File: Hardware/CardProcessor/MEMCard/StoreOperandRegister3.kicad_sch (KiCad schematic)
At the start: 3 parts, among them U15 74ABT16245

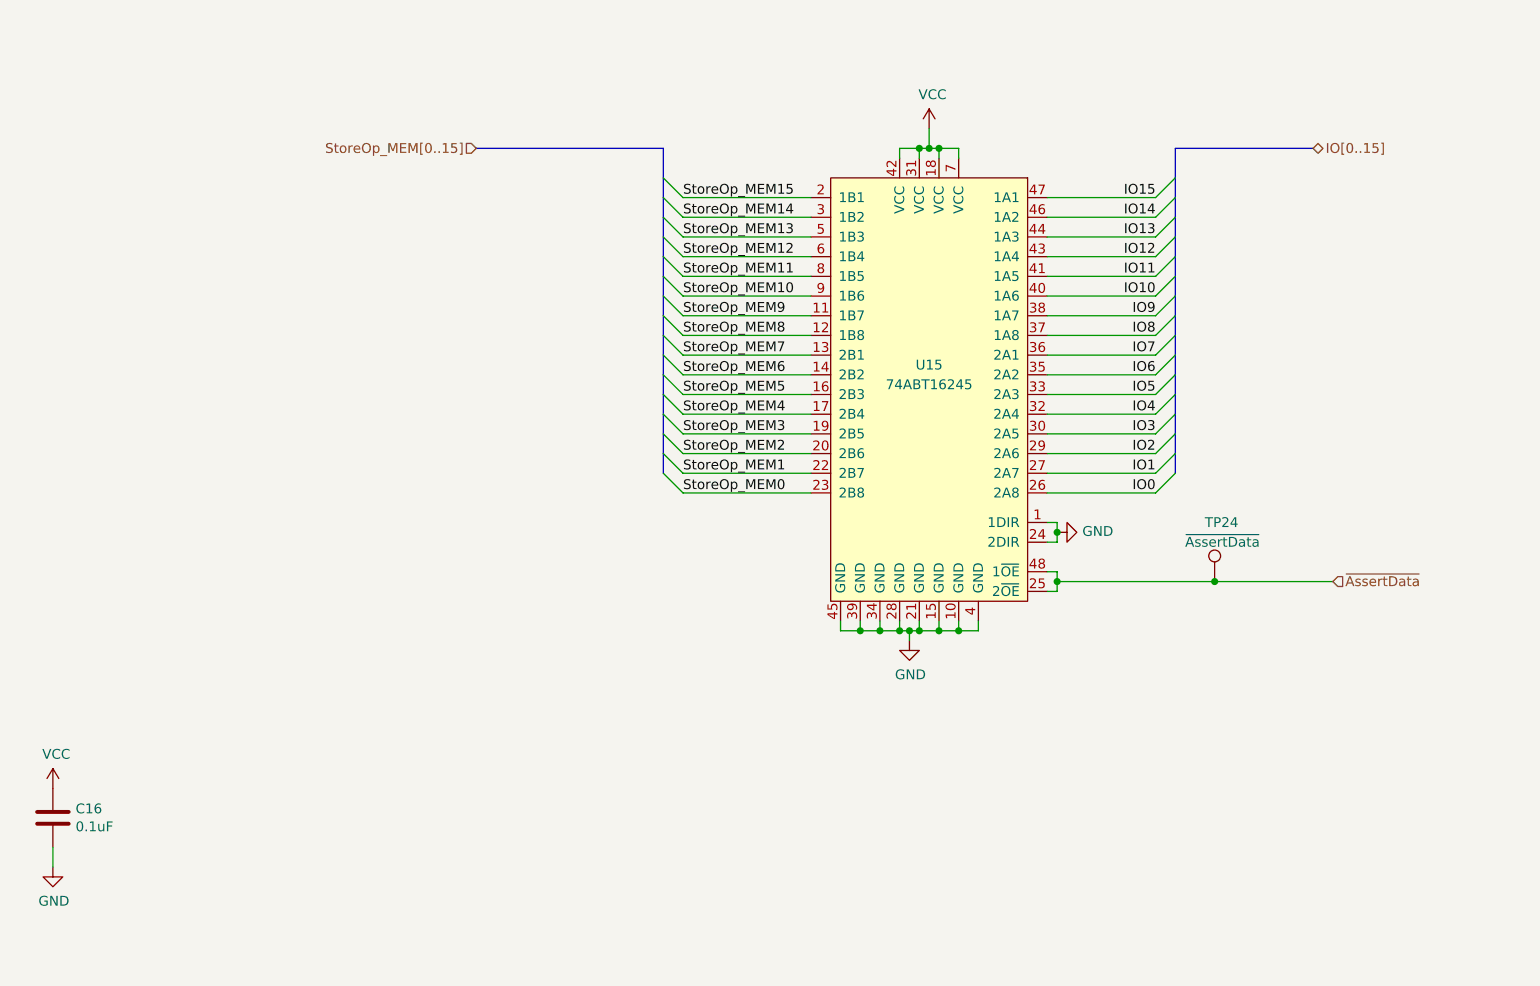
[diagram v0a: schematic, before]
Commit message: Rename MEMModule to MEMCard
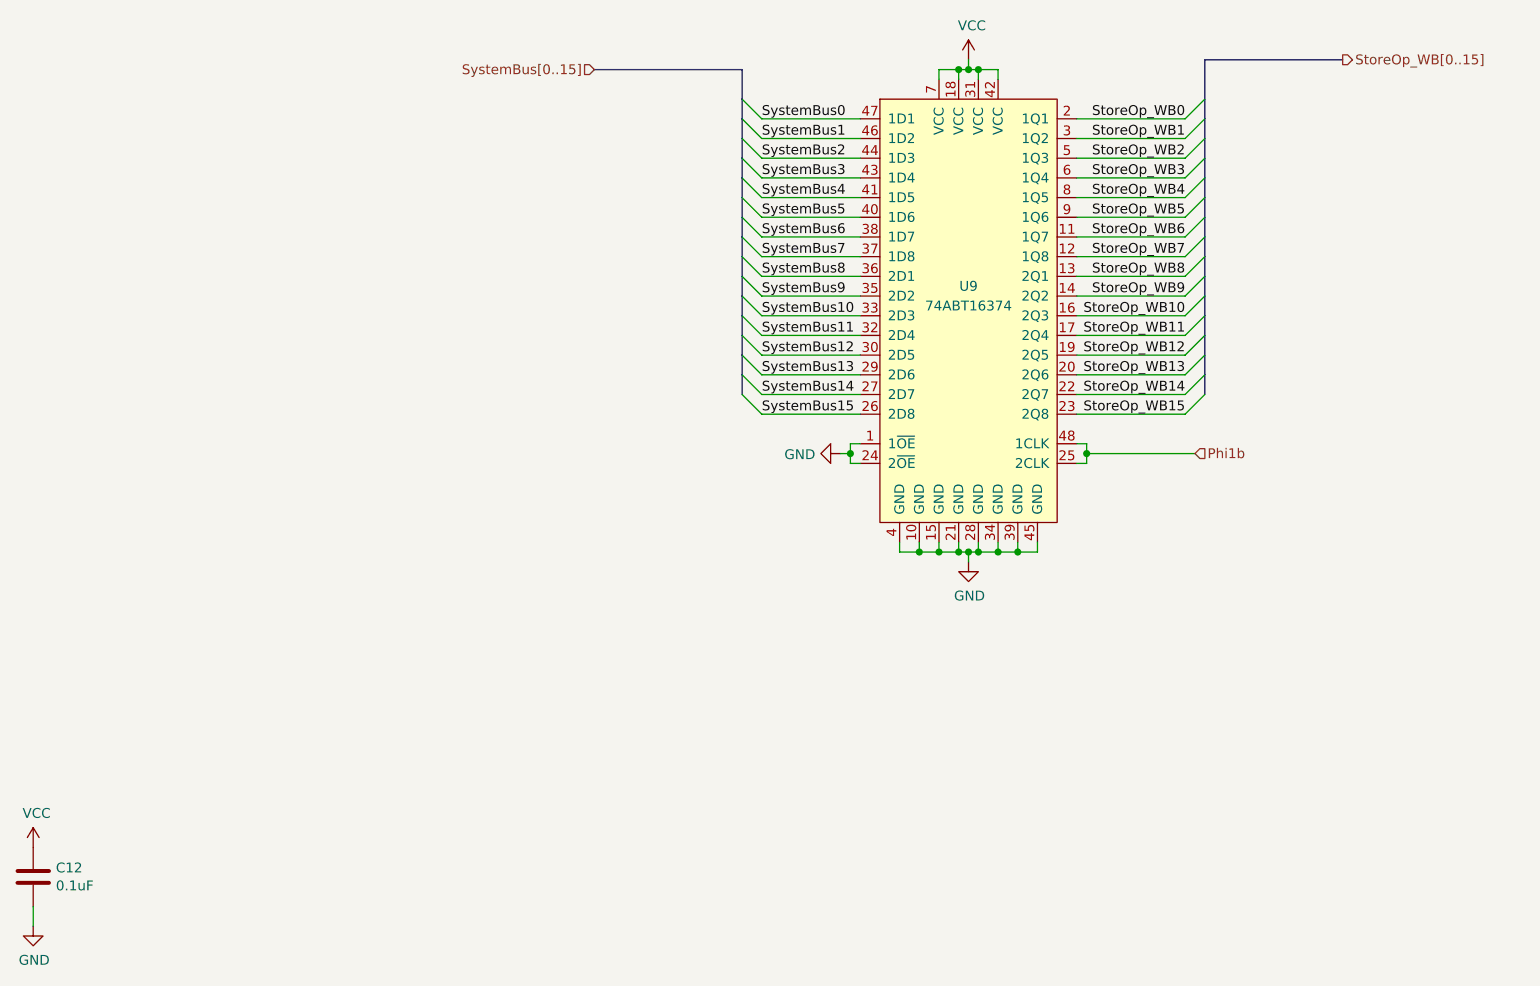
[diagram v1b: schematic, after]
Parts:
- removed C16: 0.1uF, Capacitor_SMD:C_0603_1608Metric, symbol Device:C
- removed TP24: ~{AssertData}, TestPoint:TestPoint_Pad_D1.0mm, symbol Connector:TestPoint
- removed U15: 74ABT16245, Package_SO:TSSOP-48_6.1x12.5mm_P0.5mm, symbol Turtle16:74ABT16245
- added C12: 0.1uF, Capacitor_SMD:C_0603_1608Metric, symbol Device:C
- added U9: 74ABT16374, Package_SO:TSSOP-48_6.1x12.5mm_P0.5mm, symbol Turtle16:74ABT16374
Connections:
- net GND: now also C12.2, U9.1 (1~{OE}), U9.10 (GND), U9.15 (GND), U9.21 (GND), U9.24 (2~{OE}), U9.28 (GND), U9.34 (GND), U9.39 (GND), U9.4 (GND), U9.45 (GND)
- net VCC: now also C12.1, U9.18 (VCC), U9.31 (VCC), U9.42 (VCC), U9.7 (VCC)
- new net Phi1b: U9.25 (2CLK), U9.48 (1CLK)
- new net StoreOp_WB0: U9.2 (1Q1)
- new net StoreOp_WB1: U9.3 (1Q2)
- new net StoreOp_WB10: U9.16 (2Q3)
- new net StoreOp_WB11: U9.17 (2Q4)
- new net StoreOp_WB12: U9.19 (2Q5)
- new net StoreOp_WB13: U9.20 (2Q6)
- new net StoreOp_WB14: U9.22 (2Q7)
- new net StoreOp_WB15: U9.23 (2Q8)
- new net StoreOp_WB2: U9.5 (1Q3)
- new net StoreOp_WB3: U9.6 (1Q4)
- new net StoreOp_WB4: U9.8 (1Q5)
- new net StoreOp_WB5: U9.9 (1Q6)
- new net StoreOp_WB6: U9.11 (1Q7)
- new net StoreOp_WB7: U9.12 (1Q8)
- new net StoreOp_WB8: U9.13 (2Q1)
- new net StoreOp_WB9: U9.14 (2Q2)
- new net SystemBus0: U9.47 (1D1)
- new net SystemBus1: U9.46 (1D2)
- new net SystemBus10: U9.33 (2D3)
- new net SystemBus11: U9.32 (2D4)
- new net SystemBus12: U9.30 (2D5)
- new net SystemBus13: U9.29 (2D6)
- new net SystemBus14: U9.27 (2D7)
- new net SystemBus15: U9.26 (2D8)
- new net SystemBus2: U9.44 (1D3)
- new net SystemBus3: U9.43 (1D4)
- new net SystemBus4: U9.41 (1D5)
- new net SystemBus5: U9.40 (1D6)
- new net SystemBus6: U9.38 (1D7)
- new net SystemBus7: U9.37 (1D8)
- new net SystemBus8: U9.36 (2D1)
- new net SystemBus9: U9.35 (2D2)
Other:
- title: MEM: Buffer StoreOp -> MEM/WB: Store Operand Register

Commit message: Add Turtle16Computer, a KiCad project which has schematics for the computer as a whole
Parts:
- renumbered C12 to C9
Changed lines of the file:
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@@
 		(on_board yes)
 		(dnp no)
-		(property "Reference" "C12"
+		(property "Reference" "C?"
 			(at 24.511 180.4416 0)
 			(effects
@@
 		)
 		(instances
-			(project "MEMModule"
-				(path "/0734fc7f-a6cc-4e6e-9f39-47607536bc96/f77653f6-20ed-4160-b6ab-9e3d62667a68/00000000-0000-0000-0000-00005fd56bfa"
-					(reference "C12")
-					(unit 1)
-				)
-			)
-			(project "MainBoard"
-				(path "/83c5181e-f5ee-453c-ae5c-d7256ba8837d/278b84b0-d28f-4248-8f63-f89f14b1dc97/f77653f6-20ed-4160-b6ab-9e3d62667a68/00000000-0000-0000-0000-00005fd56bfa"
+			(project "MEMCard"
+				(path "/0734fc7f-a6cc-4e6e-9f39-47607536bc96/15226c01-8e12-4b81-9562-5f5a5e30fa57/689a64e6-039c-45af-97e3-58741a934fce/00000000-0000-0000-0000-00005fd56bfa"
+					(reference "C9")
+					(unit 1)
+				)
+			)
+			(project "MEMCard"
+				(path "/83c5181e-f5ee-453c-ae5c-d7256ba8837d/278b84b0-d28f-4248-8f63-f89f14b1dc97/689a64e6-039c-45af-97e3-58741a934fce/00000000-0000-0000-0000-00005fd56bfa"
 					(reference "C?")
 					(unit 1)
@@
 		(on_board yes)
 		(dnp no)
-		(property "Reference" "#PWR075"
+		(property "Reference" "#PWR?"
 			(at 21.59 181.61 0)
 			(effects
@@
 		)
 		(instances
-			(project "MEMModule"
-				(path "/0734fc7f-a6cc-4e6e-9f39-47607536bc96/f77653f6-20ed-4160-b6ab-9e3d62667a68/00000000-0000-0000-0000-00005fd56bfa"
-					(reference "#PWR075")
-					(unit 1)
-				)
-			)
-			(project "MainBoard"
-				(path "/83c5181e-f5ee-453c-ae5c-d7256ba8837d/278b84b0-d28f-4248-8f63-f89f14b1dc97/f77653f6-20ed-4160-b6ab-9e3d62667a68/00000000-0000-0000-0000-00005fd56bfa"
+			(project "MEMCard"
+				(path "/0734fc7f-a6cc-4e6e-9f39-47607536bc96/15226c01-8e12-4b81-9562-5f5a5e30fa57/689a64e6-039c-45af-97e3-58741a934fce/00000000-0000-0000-0000-00005fd56bfa"
+					(reference "#PWR046")
+					(unit 1)
+				)
+			)
+			(project "MEMCard"
+				(path "/83c5181e-f5ee-453c-ae5c-d7256ba8837d/278b84b0-d28f-4248-8f63-f89f14b1dc97/689a64e6-039c-45af-97e3-58741a934fce/00000000-0000-0000-0000-00005fd56bfa"
 					(reference "#PWR?")
 					(unit 1)
@@
 		(on_board yes)
 		(dnp no)
-		(property "Reference" "#PWR076"
+		(property "Reference" "#PWR?"
 			(at 21.59 194.31 0)
 			(effects
@@
 		)
 		(instances
-			(project "MEMModule"
-				(path "/0734fc7f-a6cc-4e6e-9f39-47607536bc96/f77653f6-20ed-4160-b6ab-9e3d62667a68/00000000-0000-0000-0000-00005fd56bfa"
-					(reference "#PWR076")
-					(unit 1)
-				)
-			)
-			(project "MainBoard"
-				(path "/83c5181e-f5ee-453c-ae5c-d7256ba8837d/278b84b0-d28f-4248-8f63-f89f14b1dc97/f77653f6-20ed-4160-b6ab-9e3d62667a68/00000000-0000-0000-0000-00005fd56bfa"
+			(project "MEMCard"
+				(path "/0734fc7f-a6cc-4e6e-9f39-47607536bc96/15226c01-8e12-4b81-9562-5f5a5e30fa57/689a64e6-039c-45af-97e3-58741a934fce/00000000-0000-0000-0000-00005fd56bfa"
+					(reference "#PWR047")
+					(unit 1)
+				)
+			)
+			(project "MEMCard"
+				(path "/83c5181e-f5ee-453c-ae5c-d7256ba8837d/278b84b0-d28f-4248-8f63-f89f14b1dc97/689a64e6-039c-45af-97e3-58741a934fce/00000000-0000-0000-0000-00005fd56bfa"
 					(reference "#PWR?")
 					(unit 1)
@@
 		(on_board yes)
 		(dnp no)
-		(property "Reference" "#PWR077"
+		(property "Reference" "#PWR?"
 			(at 119.38 127 0)
 			(effects
@@
 		)
 		(instances
-			(project "MEMModule"
-				(path "/0734fc7f-a6cc-4e6e-9f39-47607536bc96/f77653f6-20ed-4160-b6ab-9e3d62667a68/00000000-0000-0000-0000-00005fd56bfa"
-					(reference "#PWR077")
-					(unit 1)
-				)
-			)
-			(project "MainBoard"
-				(path "/83c5181e-f5ee-453c-ae5c-d7256ba8837d/278b84b0-d28f-4248-8f63-f89f14b1dc97/f77653f6-20ed-4160-b6ab-9e3d62667a68/00000000-0000-0000-0000-00005fd56bfa"
+			(project "MEMCard"
+				(path "/0734fc7f-a6cc-4e6e-9f39-47607536bc96/15226c01-8e12-4b81-9562-5f5a5e30fa57/689a64e6-039c-45af-97e3-58741a934fce/00000000-0000-0000-0000-00005fd56bfa"
+					(reference "#PWR048")
+					(unit 1)
+				)
+			)
+			(project "MEMCard"
+				(path "/83c5181e-f5ee-453c-ae5c-d7256ba8837d/278b84b0-d28f-4248-8f63-f89f14b1dc97/689a64e6-039c-45af-97e3-58741a934fce/00000000-0000-0000-0000-00005fd56bfa"
 					(reference "#PWR?")
 					(unit 1)
@@
 		(on_board yes)
 		(dnp no)
-		(property "Reference" "#PWR078"
+		(property "Reference" "#PWR?"
 			(at 142.24 80.01 0)
 			(effects
@@
 		)
 		(instances
-			(project "MEMModule"
-				(path "/0734fc7f-a6cc-4e6e-9f39-47607536bc96/f77653f6-20ed-4160-b6ab-9e3d62667a68/00000000-0000-0000-0000-00005fd56bfa"
-					(reference "#PWR078")
-					(unit 1)
-				)
-			)
-			(project "MainBoard"
-				(path "/83c5181e-f5ee-453c-ae5c-d7256ba8837d/278b84b0-d28f-4248-8f63-f89f14b1dc97/f77653f6-20ed-4160-b6ab-9e3d62667a68/00000000-0000-0000-0000-00005fd56bfa"
+			(project "MEMCard"
+				(path "/0734fc7f-a6cc-4e6e-9f39-47607536bc96/15226c01-8e12-4b81-9562-5f5a5e30fa57/689a64e6-039c-45af-97e3-58741a934fce/00000000-0000-0000-0000-00005fd56bfa"
+					(reference "#PWR049")
+					(unit 1)
+				)
+			)
+			(project "MEMCard"
+				(path "/83c5181e-f5ee-453c-ae5c-d7256ba8837d/278b84b0-d28f-4248-8f63-f89f14b1dc97/689a64e6-039c-45af-97e3-58741a934fce/00000000-0000-0000-0000-00005fd56bfa"
 					(reference "#PWR?")
 					(unit 1)
@@
 		(on_board yes)
 		(dnp no)
-		(property "Reference" "#PWR079"
+		(property "Reference" "#PWR?"
 			(at 142.24 147.32 0)
 			(effects
@@
 		)
 		(instances
-			(project "MEMModule"
-				(path "/0734fc7f-a6cc-4e6e-9f39-47607536bc96/f77653f6-20ed-4160-b6ab-9e3d62667a68/00000000-0000-0000-0000-00005fd56bfa"
-					(reference "#PWR079")
-					(unit 1)
-				)
-			)
-			(project "MainBoard"
-				(path "/83c5181e-f5ee-453c-ae5c-d7256ba8837d/278b84b0-d28f-4248-8f63-f89f14b1dc97/f77653f6-20ed-4160-b6ab-9e3d62667a68/00000000-0000-0000-0000-00005fd56bfa"
+			(project "MEMCard"
+				(path "/0734fc7f-a6cc-4e6e-9f39-47607536bc96/15226c01-8e12-4b81-9562-5f5a5e30fa57/689a64e6-039c-45af-97e3-58741a934fce/00000000-0000-0000-0000-00005fd56bfa"
+					(reference "#PWR050")
+					(unit 1)
+				)
+			)
+			(project "MEMCard"
+				(path "/83c5181e-f5ee-453c-ae5c-d7256ba8837d/278b84b0-d28f-4248-8f63-f89f14b1dc97/689a64e6-039c-45af-97e3-58741a934fce/00000000-0000-0000-0000-00005fd56bfa"
 					(reference "#PWR?")
 					(unit 1)
@@
 		(on_board yes)
 		(dnp no)
-		(property "Reference" "U9"
+		(property "Reference" "U?"
 			(at 142.24 105.41 0)
 			(effects
@@
 		)
 		(instances
-			(project "MEMModule"
-				(path "/0734fc7f-a6cc-4e6e-9f39-47607536bc96/f77653f6-20ed-4160-b6ab-9e3d62667a68/00000000-0000-0000-0000-00005fd56bfa"
+			(project "MEMCard"
+				(path "/0734fc7f-a6cc-4e6e-9f39-47607536bc96/15226c01-8e12-4b81-9562-5f5a5e30fa57/689a64e6-039c-45af-97e3-58741a934fce/00000000-0000-0000-0000-00005fd56bfa"
 					(reference "U9")
 					(unit 1)
 				)
 			)
-			(project "MainBoard"
-				(path "/83c5181e-f5ee-453c-ae5c-d7256ba8837d/278b84b0-d28f-4248-8f63-f89f14b1dc97/f77653f6-20ed-4160-b6ab-9e3d62667a68/00000000-0000-0000-0000-00005fd56bfa"
+			(project "MEMCard"
+				(path "/83c5181e-f5ee-453c-ae5c-d7256ba8837d/278b84b0-d28f-4248-8f63-f89f14b1dc97/689a64e6-039c-45af-97e3-58741a934fce/00000000-0000-0000-0000-00005fd56bfa"
 					(reference "U?")
 					(unit 1)

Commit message: Annotate schematics such that Turtle16Computer can perform ERC and DRC
- Turtle16Computer must be fully annotated to perform ERC on the schematic.
Also, the PCB cannot be updated without full annotations either. However,
KiCad projects for individual PCBs must also remain annotated and capable
of updating the PCB and performing ERC and DRC.

- Manually set KiCad project fields to "" in kicad_sch files

- Manually replace the UUID of EXCard so it no longer collides with the
UUI of the Turtle16Computer project.
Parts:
- renumbered C9 to C41, U9 to U36
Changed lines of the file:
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@@
 		(on_board yes)
 		(dnp no)
-		(property "Reference" "C?"
+		(property "Reference" "C41"
 			(at 24.511 180.4416 0)
 			(effects
@@
 		)
 		(instances
-			(project "MEMCard"
+			(project ""
 				(path "/0734fc7f-a6cc-4e6e-9f39-47607536bc96/15226c01-8e12-4b81-9562-5f5a5e30fa57/689a64e6-039c-45af-97e3-58741a934fce/00000000-0000-0000-0000-00005fd56bfa"
-					(reference "C9")
+					(reference "C6")
 					(unit 1)
 				)
@@
 			(project "Turtle16Computer"
 				(path "/83c5181e-f5ee-453c-ae5c-d7256ba8837d/278b84b0-d28f-4248-8f63-f89f14b1dc97/689a64e6-039c-45af-97e3-58741a934fce/00000000-0000-0000-0000-00005fd56bfa"
-					(reference "C?")
+					(reference "C41")
 					(unit 1)
 				)
@@
 		(on_board yes)
 		(dnp no)
-		(property "Reference" "#PWR?"
+		(property "Reference" "#PWR0669"
 			(at 21.59 181.61 0)
 			(effects
@@
 		)
 		(instances
-			(project "MEMCard"
+			(project ""
 				(path "/0734fc7f-a6cc-4e6e-9f39-47607536bc96/15226c01-8e12-4b81-9562-5f5a5e30fa57/689a64e6-039c-45af-97e3-58741a934fce/00000000-0000-0000-0000-00005fd56bfa"
-					(reference "#PWR046")
+					(reference "#PWR026")
 					(unit 1)
 				)
@@
 			(project "Turtle16Computer"
 				(path "/83c5181e-f5ee-453c-ae5c-d7256ba8837d/278b84b0-d28f-4248-8f63-f89f14b1dc97/689a64e6-039c-45af-97e3-58741a934fce/00000000-0000-0000-0000-00005fd56bfa"
-					(reference "#PWR?")
+					(reference "#PWR0669")
 					(unit 1)
 				)
@@
 		(on_board yes)
 		(dnp no)
-		(property "Reference" "#PWR?"
+		(property "Reference" "#PWR0670"
 			(at 21.59 194.31 0)
 			(effects
@@
 		)
 		(instances
-			(project "MEMCard"
+			(project ""
 				(path "/0734fc7f-a6cc-4e6e-9f39-47607536bc96/15226c01-8e12-4b81-9562-5f5a5e30fa57/689a64e6-039c-45af-97e3-58741a934fce/00000000-0000-0000-0000-00005fd56bfa"
-					(reference "#PWR047")
+					(reference "#PWR027")
 					(unit 1)
 				)
@@
 			(project "Turtle16Computer"
 				(path "/83c5181e-f5ee-453c-ae5c-d7256ba8837d/278b84b0-d28f-4248-8f63-f89f14b1dc97/689a64e6-039c-45af-97e3-58741a934fce/00000000-0000-0000-0000-00005fd56bfa"
-					(reference "#PWR?")
+					(reference "#PWR0670")
 					(unit 1)
 				)
@@
 		(on_board yes)
 		(dnp no)
-		(property "Reference" "#PWR?"
+		(property "Reference" "#PWR0667"
 			(at 119.38 127 0)
 			(effects
@@
 		)
 		(instances
-			(project "MEMCard"
+			(project ""
 				(path "/0734fc7f-a6cc-4e6e-9f39-47607536bc96/15226c01-8e12-4b81-9562-5f5a5e30fa57/689a64e6-039c-45af-97e3-58741a934fce/00000000-0000-0000-0000-00005fd56bfa"
-					(reference "#PWR048")
+					(reference "#PWR028")
 					(unit 1)
 				)
@@
 			(project "Turtle16Computer"
 				(path "/83c5181e-f5ee-453c-ae5c-d7256ba8837d/278b84b0-d28f-4248-8f63-f89f14b1dc97/689a64e6-039c-45af-97e3-58741a934fce/00000000-0000-0000-0000-00005fd56bfa"
-					(reference "#PWR?")
+					(reference "#PWR0667")
 					(unit 1)
 				)
@@
 		(on_board yes)
 		(dnp no)
-		(property "Reference" "#PWR?"
+		(property "Reference" "#PWR0666"
 			(at 142.24 80.01 0)
 			(effects
@@
 		)
 		(instances
-			(project "MEMCard"
+			(project ""
 				(path "/0734fc7f-a6cc-4e6e-9f39-47607536bc96/15226c01-8e12-4b81-9562-5f5a5e30fa57/689a64e6-039c-45af-97e3-58741a934fce/00000000-0000-0000-0000-00005fd56bfa"
-					(reference "#PWR049")
+					(reference "#PWR029")
 					(unit 1)
 				)
@@
 			(project "Turtle16Computer"
 				(path "/83c5181e-f5ee-453c-ae5c-d7256ba8837d/278b84b0-d28f-4248-8f63-f89f14b1dc97/689a64e6-039c-45af-97e3-58741a934fce/00000000-0000-0000-0000-00005fd56bfa"
-					(reference "#PWR?")
+					(reference "#PWR0666")
 					(unit 1)
 				)
@@
 		(on_board yes)
 		(dnp no)
-		(property "Reference" "#PWR?"
+		(property "Reference" "#PWR0668"
 			(at 142.24 147.32 0)
 			(effects
@@
 		)
 		(instances
-			(project "MEMCard"
+			(project ""
 				(path "/0734fc7f-a6cc-4e6e-9f39-47607536bc96/15226c01-8e12-4b81-9562-5f5a5e30fa57/689a64e6-039c-45af-97e3-58741a934fce/00000000-0000-0000-0000-00005fd56bfa"
-					(reference "#PWR050")
+					(reference "#PWR030")
 					(unit 1)
 				)
@@
 			(project "Turtle16Computer"
 				(path "/83c5181e-f5ee-453c-ae5c-d7256ba8837d/278b84b0-d28f-4248-8f63-f89f14b1dc97/689a64e6-039c-45af-97e3-58741a934fce/00000000-0000-0000-0000-00005fd56bfa"
-					(reference "#PWR?")
+					(reference "#PWR0668")
 					(unit 1)
 				)
@@
 		(on_board yes)
 		(dnp no)
-		(property "Reference" "U?"
+		(property "Reference" "U36"
 			(at 142.24 105.41 0)
 			(effects
@@
 		)
 		(instances
-			(project "MEMCard"
+			(project ""
 				(path "/0734fc7f-a6cc-4e6e-9f39-47607536bc96/15226c01-8e12-4b81-9562-5f5a5e30fa57/689a64e6-039c-45af-97e3-58741a934fce/00000000-0000-0000-0000-00005fd56bfa"
-					(reference "U9")
+					(reference "U6")
 					(unit 1)
 				)
@@
 			(project "Turtle16Computer"
 				(path "/83c5181e-f5ee-453c-ae5c-d7256ba8837d/278b84b0-d28f-4248-8f63-f89f14b1dc97/689a64e6-039c-45af-97e3-58741a934fce/00000000-0000-0000-0000-00005fd56bfa"
-					(reference "U?")
-					(unit 1)
-				)
+					(reference "U36")
+					(unit 1)
+				)

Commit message: Ensure all cards have a unique 4-bit identifier code and proper power pins
The pinout on all cards will devote the first four pins to the identifier,
followed by four pins for +5V, and four pins for GND. This allows a card to
draw up to about 2 amps.
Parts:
- renumbered C41 to C6, U36 to U6
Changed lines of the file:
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@@
 		(on_board yes)
 		(dnp no)
-		(property "Reference" "C41"
+		(property "Reference" "C6"
 			(at 24.511 180.4416 0)
 			(effects
@@
 		(on_board yes)
 		(dnp no)
-		(property "Reference" "#PWR0669"
+		(property "Reference" "#PWR026"
 			(at 21.59 181.61 0)
 			(effects
@@
 		(on_board yes)
 		(dnp no)
-		(property "Reference" "#PWR0670"
+		(property "Reference" "#PWR027"
 			(at 21.59 194.31 0)
 			(effects
@@
 		(on_board yes)
 		(dnp no)
-		(property "Reference" "#PWR0667"
+		(property "Reference" "#PWR028"
 			(at 119.38 127 0)
 			(effects
@@
 		(on_board yes)
 		(dnp no)
-		(property "Reference" "#PWR0666"
+		(property "Reference" "#PWR029"
 			(at 142.24 80.01 0)
 			(effects
@@
 		(on_board yes)
 		(dnp no)
-		(property "Reference" "#PWR0668"
+		(property "Reference" "#PWR030"
 			(at 142.24 147.32 0)
 			(effects
@@
 		(on_board yes)
 		(dnp no)
-		(property "Reference" "U36"
+		(property "Reference" "U6"
 			(at 142.24 105.41 0)
 			(effects
